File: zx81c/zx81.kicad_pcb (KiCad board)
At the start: 2 copper layers, 142 x 100 mm, 78 parts, among them IC1 ZX81ULA, IC2 27C512, IC2B0 ZXROM-SMALL, IC3 Z80CPU, IC4 62256, IC4A0 2114, IC4B0 2114, K1 ZX81CONN, K2 MIC, K3 EAR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

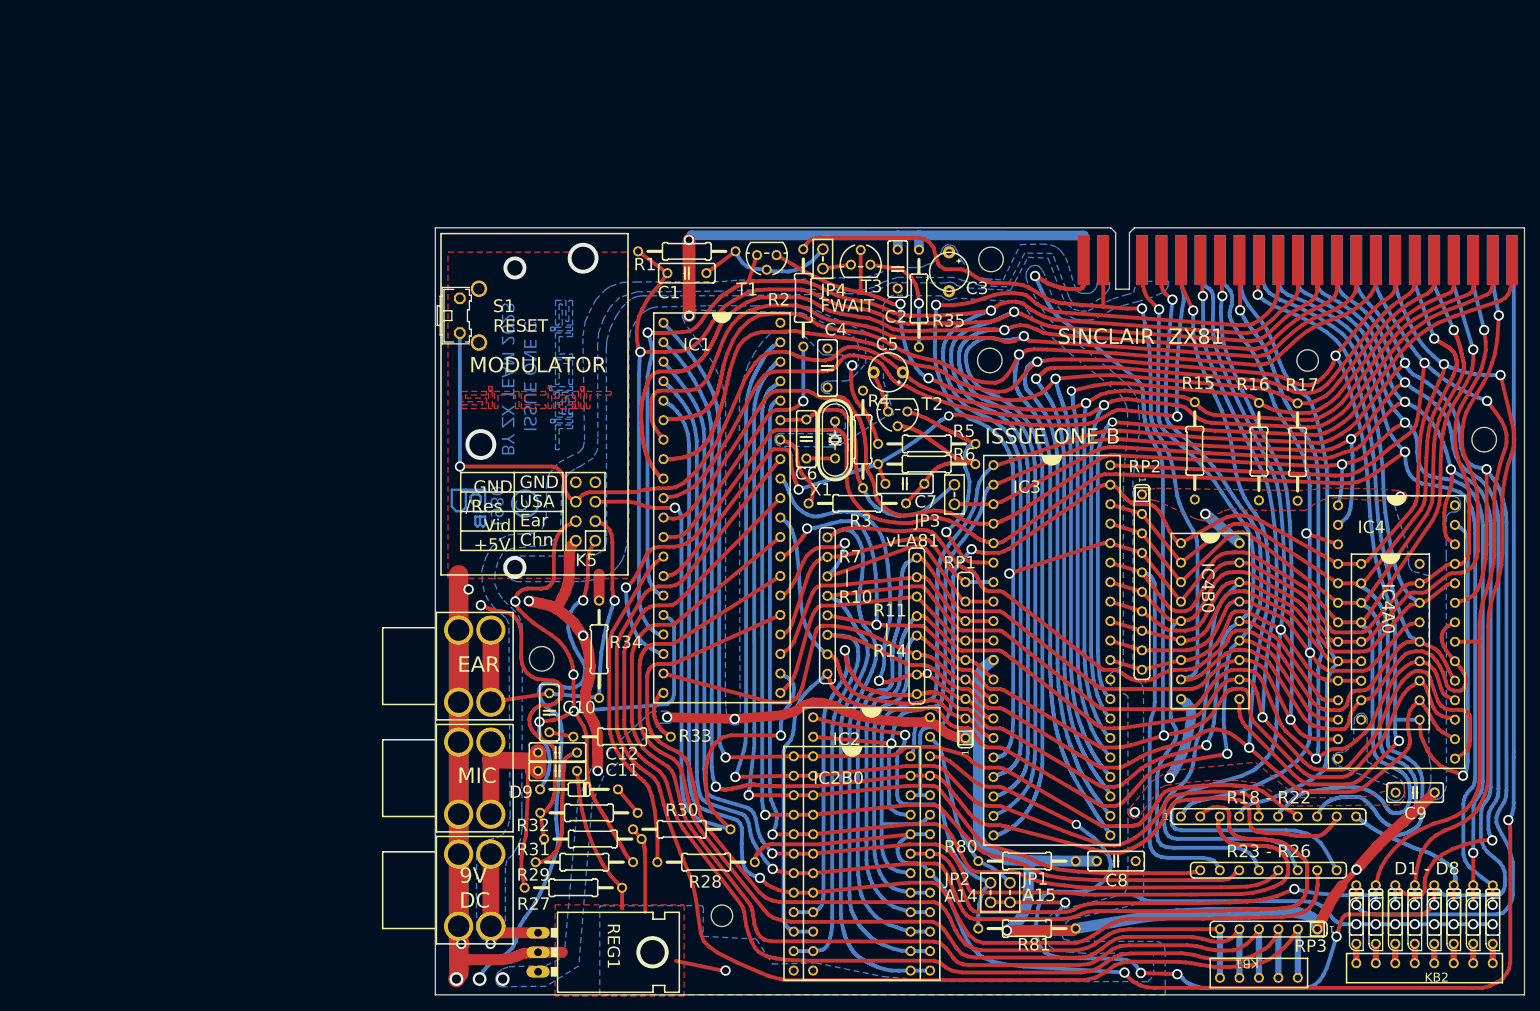
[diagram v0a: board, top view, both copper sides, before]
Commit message: updated schematic and pcb to include project credits
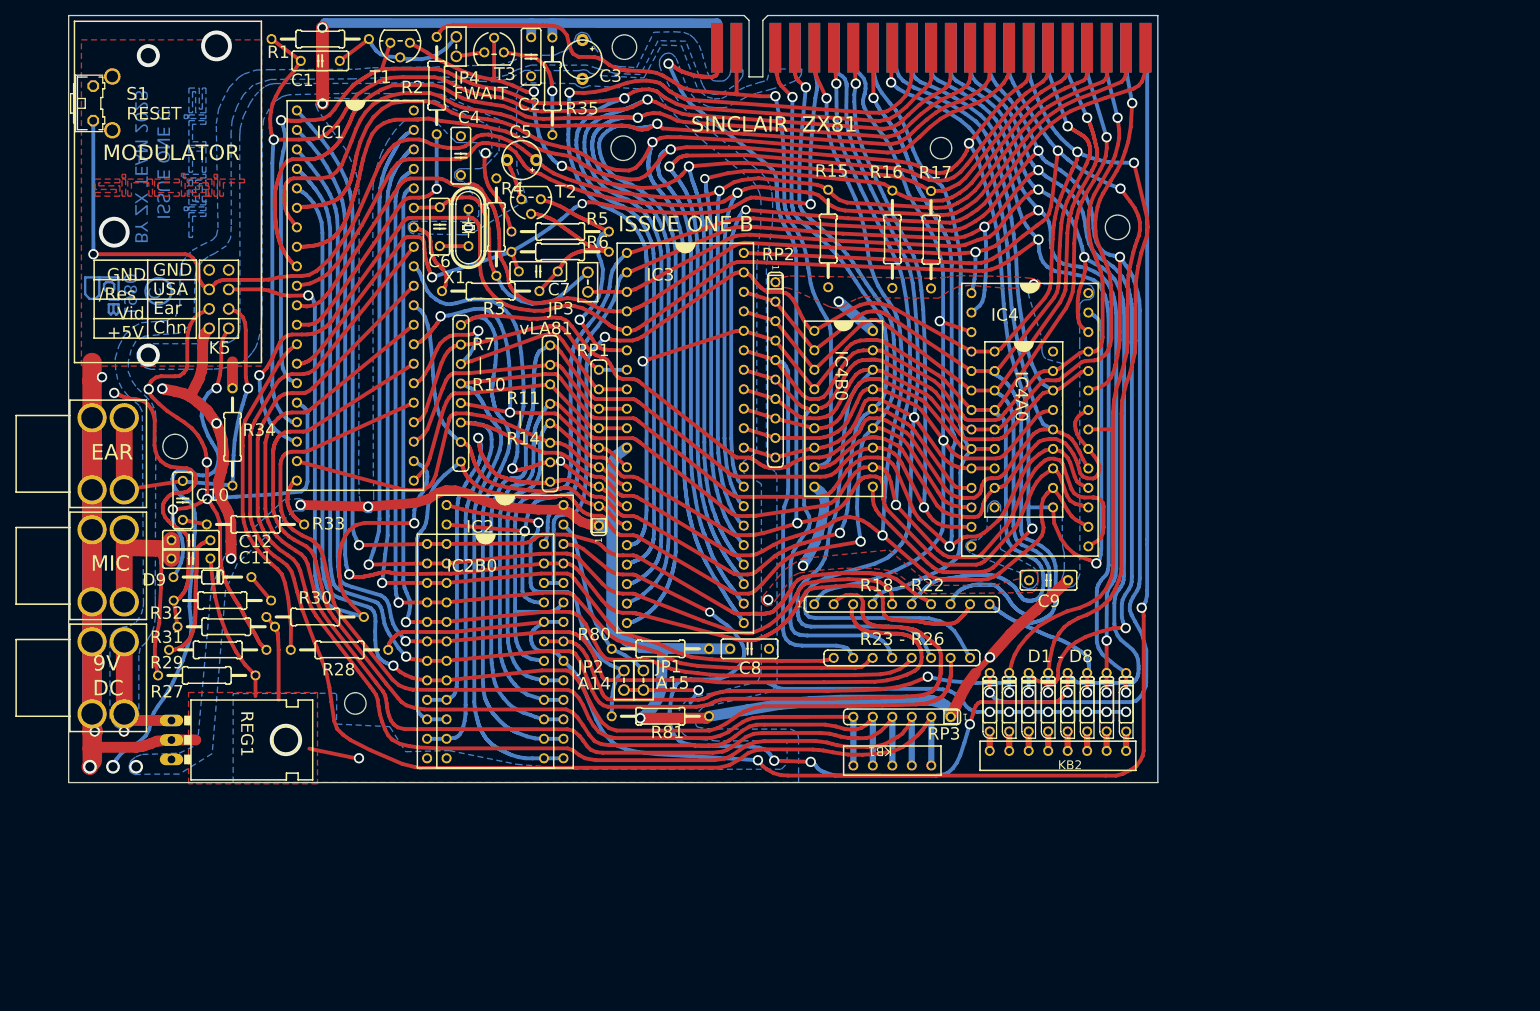
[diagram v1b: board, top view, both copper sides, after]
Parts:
- D9: value (none) -> not used
- moved D2 55.2 mm to (152.3, 116.9)
- moved D3 55.2 mm to (154.9, 116.9)
- moved D4 55.2 mm to (157.4, 116.9)
- moved D6 55.2 mm to (162.5, 116.9)
- moved D7 55.2 mm to (165.0, 116.9)
- moved D8 55.2 mm to (167.6, 116.9)
- moved IC2B0 55.2 mm to (84.1, 110.2)
- moved IC4 55.2 mm to (155.0, 77.5)
- moved IC4B0 55.2 mm to (130.7, 78.6)
- moved KB1 55.2 mm to (137.1, 125.1)
- moved KB2 55.2 mm to (158.7, 123.2)
- moved RP1 55.2 mm to (98.8, 83.7)
- moved RP4 55.2 mm to (80.8, 76.6)
- moved RP6 55.2 mm to (138.3, 111.1)
- moved RP7 55.2 mm to (138.3, 104.1)
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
